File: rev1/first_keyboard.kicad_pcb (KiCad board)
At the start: 2 copper layers, 300 x 88.1 mm, 83 parts, among them SW1 SW_Push, SW10 SW_Push, SW11 SW_Push, SW12 SW_Push, SW13 SW_Push, SW14 SW_Push, SW15 SW_Push, SW16 SW_Push, SW17 SW_Push, SW18 SW_Push, SW19 SW_Push, SW2 SW_Push, SW20 SW_Push, SW21 SW_Push, SW22 SW_Push, SW23 SW_Push, SW24 SW_Push, SW25 SW_Push, SW26 SW_Push, SW27 SW_Push, SW28 SW_Push, SW29 SW_Push, SW3 SW_Push, SW30 SW_Push, SW31 SW_Push, SW32 SW_Push, SW33 SW_Push, SW34 SW_Push, SW35 SW_Push, SW36 SW_Push, SW37 SW_Push, SW38 SW_Push, SW39 SW_Push, SW4 SW_Push, SW40 SW_Push, SW41 SW_Push, SW5 SW_Push, SW6 SW_Push, SW7 SW_Push, SW8 SW_Push, SW9 SW_Push, U1 Pico

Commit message: feat: ダイオード位置変更
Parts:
- moved D41 7.31 mm to (357.2, 167.6)
- moved D22 2.85 mm to (266.7, 134.3)
- moved D23 2.85 mm to (266.7, 153.4)
- moved D24 2.85 mm to (266.7, 172.4)
- moved D27 2.85 mm to (285.8, 148.6)
- moved D30 2.85 mm to (285.8, 186.7)
- moved D40 2.85 mm to (361.9, 134.3)
- moved D26 2.85 mm to (285.8, 129.5)
- moved D1 2.85 mm to (85.7, 134.3)
- moved D2 2.85 mm to (85.7, 153.4)
- moved D3 2.85 mm to (85.7, 172.4)
- moved D28 2.85 mm to (285.8, 167.6)
- moved D29 2.85 mm to (266.7, 191.5)
- moved D11 2.85 mm to (142.9, 148.6)
- moved D13 2.85 mm to (161.9, 186.7)
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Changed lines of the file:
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@@
 	(footprint "kbd_Parts:Diode_TH_SMD"
 		(layer "F.Cu")
-		(at 326.23125 147.03125 90)
+		(at 323.85 148.59 90)
 		(descr "Resitance 3 pas")
 		(tags "R")
@@
 	(footprint "kbd_Parts:Diode_TH_SMD"
 		(layer "F.Cu")
-		(at 164.30625 185.13125 90)
+		(at 161.925 186.69 90)
 		(descr "Resitance 3 pas")
 		(tags "R")
@@
 	(footprint "kbd_Parts:Diode_TH_SMD"
 		(layer "F.Cu")
-		(at 269.08125 132.74375 90)
+		(at 266.7 134.3025 90)
 		(descr "Resitance 3 pas")
 		(tags "R")
@@
 	(footprint "kbd_Parts:Diode_TH_SMD"
 		(layer "F.Cu")
-		(at 107.15625 166.08125 90)
+		(at 104.775 167.64 90)
 		(descr "Resitance 3 pas")
 		(tags "R")
@@
 	(footprint "kbd_Parts:Diode_TH_SMD"
 		(layer "F.Cu")
-		(at 183.35625 132.74375 90)
+		(at 180.975 134.3025 90)
 		(descr "Resitance 3 pas")
 		(tags "R")
@@
 	(footprint "kbd_Parts:Diode_TH_SMD"
 		(layer "F.Cu")
-		(at 145.25625 166.08125 90)
+		(at 142.875 167.64 90)
 		(descr "Resitance 3 pas")
 		(tags "R")
@@
 	(footprint "kbd_Parts:Diode_TH_SMD"
 		(layer "F.Cu")
-		(at 107.15625 127.98125 90)
+		(at 104.775 129.54 90)
 		(descr "Resitance 3 pas")
 		(tags "R")
@@
 	(footprint "kbd_Parts:Diode_TH_SMD"
 		(layer "F.Cu")
-		(at 126.20625 147.03125 90)
+		(at 123.825 148.59 90)
 		(descr "Resitance 3 pas")
 		(tags "R")
@@
 	(footprint "kbd_Parts:Diode_TH_SMD"
 		(layer "F.Cu")
-		(at 202.40625 192.275 90)
+		(at 200.025 193.83375 90)
 		(descr "Resitance 3 pas")
 		(tags "R")
@@
 	(footprint "kbd_Parts:Diode_TH_SMD"
 		(layer "F.Cu")
-		(at 88.10625 151.79375 90)
+		(at 85.725 153.3525 90)
 		(descr "Resitance 3 pas")
 		(tags "R")
@@
 	(footprint "kbd_Parts:Diode_TH_SMD"
 		(layer "F.Cu")
-		(at 126.20625 127.98125 90)
+		(at 123.825 129.54 90)
 		(descr "Resitance 3 pas")
 		(tags "R")
@@
 	(footprint "kbd_Parts:Diode_TH_SMD"
 		(layer "F.Cu")
-		(at 126.20625 166.08125 90)
+		(at 123.825 167.64 90)
 		(descr "Resitance 3 pas")
 		(tags "R")
@@
 	(footprint "kbd_Parts:Diode_TH_SMD"
 		(layer "F.Cu")
-		(at 250.03125 192.275 90)
+		(at 247.65 193.83375 90)
 		(descr "Resitance 3 pas")
 		(tags "R")
@@
 	(footprint "kbd_Parts:Diode_TH_SMD"
 		(layer "F.Cu")
-		(at 288.13125 166.08125 90)
+		(at 285.75 167.64 90)
 		(descr "Resitance 3 pas")
 		(tags "R")
@@
 	(footprint "kbd_Parts:Diode_TH_SMD"
 		(layer "F.Cu")
-		(at 88.10625 170.84375 90)
+		(at 85.725 172.4025 90)
 		(descr "Resitance 3 pas")
 		(tags "R")
@@
 	(footprint "kbd_Parts:Diode_TH_SMD"
 		(layer "F.Cu")
-		(at 183.35625 170.84375 90)
+		(at 180.975 172.4025 90)
 		(descr "Resitance 3 pas")
 		(tags "R")
@@
 	(footprint "kbd_Parts:Diode_TH_SMD"
 		(layer "F.Cu")
-		(at 164.30625 147.03125 90)
+		(at 161.925 148.59 90)
 		(descr "Resitance 3 pas")
 		(tags "R")
@@
 	(footprint "kbd_Parts:Diode_TH_SMD"
 		(layer "F.Cu")
-		(at 326.23125 166.08125 90)
+		(at 323.85 167.64 90)
 		(descr "Resitance 3 pas")
 		(tags "R")
@@
 	(footprint "kbd_Parts:Diode_TH_SMD"
 		(layer "F.Cu")
-		(at 342.9 147.03125 90)
+		(at 342.9 148.59 90)
 		(descr "Resitance 3 pas")
 		(tags "R")
@@
 	(footprint "kbd_Parts:Diode_TH_SMD"
 		(layer "F.Cu")
-		(at 145.25625 147.03125 90)
+		(at 142.875 148.59 90)
 		(descr "Resitance 3 pas")
 		(tags "R")
@@
 	(footprint "kbd_Parts:Diode_TH_SMD"
 		(layer "F.Cu")
-		(at 288.13125 147.03125 90)
+		(at 285.75 148.59 90)
 		(descr "Resitance 3 pas")
 		(tags "R")
@@
 	(footprint "kbd_Parts:Diode_TH_SMD"
 		(layer "F.Cu")
-		(at 288.13125 127.98125 90)
+		(at 285.75 129.54 90)
 		(descr "Resitance 3 pas")
 		(tags "R")
@@
 	(footprint "kbd_Parts:Diode_TH_SMD"
 		(layer "F.Cu")
-		(at 183.35625 189.89375 90)
+		(at 180.975 191.4525 90)
 		(descr "Resitance 3 pas")
 		(tags "R")
@@
 	(footprint "kbd_Parts:Diode_TH_SMD"
 		(layer "F.Cu")
-		(at 307.18125 147.03125 90)
+		(at 304.8 148.59 90)
 		(descr "Resitance 3 pas")
 		(tags "R")
@@
 	(footprint "kbd_Parts:Diode_TH_SMD"
 		(layer "F.Cu")
-		(at 342.9 127.98125 90)
+		(at 342.9 129.54 90)
 		(descr "Resitance 3 pas")
 		(tags "R")
@@
 	(footprint "kbd_Parts:Diode_TH_SMD"
 		(layer "F.Cu")
-		(at 145.25625 127.98125 90)
+		(at 142.875 129.54 90)
 		(descr "Resitance 3 pas")
 		(tags "R")
@@
 	(footprint "kbd_Parts:Diode_TH_SMD"
 		(layer "F.Cu")
-		(at 364.33125 132.74375 90)
+		(at 361.95 134.3025 90)
 		(descr "Resitance 3 pas")
 		(tags "R")
@@
 	(footprint "kbd_Parts:Diode_TH_SMD"
 		(layer "F.Cu")
-		(at 342.9 166.08125 90)
+		(at 342.9 167.64 90)
 		(descr "Resitance 3 pas")
 		(tags "R")
@@
 	(footprint "kbd_Parts:Diode_TH_SMD"
 		(layer "F.Cu")
-		(at 183.35625 151.79375 90)
+		(at 180.975 153.3525 90)
 		(descr "Resitance 3 pas")
 		(tags "R")
@@
 	(footprint "kbd_Parts:Diode_TH_SMD"
 		(layer "F.Cu")
-		(at 107.15625 147.03125 90)
+		(at 104.775 148.59 90)
 		(descr "Resitance 3 pas")
 		(tags "R")
@@
 	(footprint "kbd_Parts:Diode_TH_SMD"
 		(layer "F.Cu")
-		(at 307.18125 127.98125 90)
+		(at 304.8 129.54 90)
 		(descr "Resitance 3 pas")
 		(tags "R")
@@
 	(footprint "kbd_Parts:Diode_TH_SMD"
 		(layer "F.Cu")
-		(at 326.23125 127.98125 90)
+		(at 323.85 129.54 90)
 		(descr "Resitance 3 pas")
 		(tags "R")
@@
 	(footprint "kbd_Parts:Diode_TH_SMD"
 		(layer "F.Cu")
-		(at 88.10625 132.74375 90)
+		(at 85.725 134.3025 90)
 		(descr "Resitance 3 pas")
 		(tags "R")
@@
 	(footprint "kbd_Parts:Diode_TH_SMD"
 		(layer "F.Cu")
-		(at 307.18125 166.08125 90)
+		(at 304.8 167.64 90)
 		(descr "Resitance 3 pas")
 		(tags "R")
@@
 	(footprint "kbd_Parts:Diode_TH_SMD"
 		(layer "F.Cu")
-		(at 269.08125 170.84375 90)
+		(at 266.7 172.4025 90)
 		(descr "Resitance 3 pas")
 		(tags "R")
@@
 	(footprint "kbd_Parts:Diode_TH_SMD"
 		(layer "F.Cu")
-		(at 269.08125 189.89375 90)
+		(at 266.7 191.4525 90)
 		(descr "Resitance 3 pas")
 		(tags "R")
@@
 	(footprint "kbd_Parts:Diode_TH_SMD"
 		(layer "F.Cu")
-		(at 269.08125 151.79375 90)
+		(at 266.7 153.3525 90)
 		(descr "Resitance 3 pas")
 		(tags "R")
@@
 	(footprint "kbd_Parts:Diode_TH_SMD"
 		(layer "F.Cu")
-		(at 164.30625 127.98125 90)
+		(at 161.925 129.54 90)
 		(descr "Resitance 3 pas")
 		(tags "R")
@@
 	(footprint "kbd_Parts:Diode_TH_SMD"
 		(layer "F.Cu")
-		(at 364.33125 166.08125 90)
+		(at 357.1875 167.64 90)
 		(descr "Resitance 3 pas")
 		(tags "R")
@@
 	(footprint "kbd_Parts:Diode_TH_SMD"
 		(layer "F.Cu")
-		(at 164.30625 166.08125 90)
+		(at 161.925 167.64 90)
 		(descr "Resitance 3 pas")
 		(tags "R")
@@
 	(footprint "kbd_Parts:Diode_TH_SMD"
 		(layer "F.Cu")
-		(at 288.13125 185.13125 90)
+		(at 285.75 186.69 90)
 		(descr "Resitance 3 pas")
 		(tags "R")
@@
 		(layer "Edge.Cuts")
 	)
-	(dimension
-		(type aligned)
-		(layer "F.Cu")
-		(pts
-			(xy 250.03125 138.1125) (xy 216.69375 138.1125)
-		)
-		(height 0)
-		(gr_text "33.3375 mm"
-			(at 233.3625 136.3125 0)
-			(layer "F.Cu")
-			(effects
-				(font
-					(size 1.5 1.5)
-					(thickness 0.3)
-				)
-			)
-		)
-		(format
-			(prefix "")
-			(suffix "")
-			(units 3)
-			(units_format 1)
-			(precision 4)
-		)
-		(style
-			(thickness 0.2)
-			(arrow_length 1.27)
-			(text_position_mode 0)
-			(extension_height 0.58642)
-			(extension_offset 0.5) keep_text_aligned)
-	)
-	(dimension
-		(type aligned)
-		(layer "F.Cu")
-		(pts
-			(xy 183.35625 138.1125) (xy 216.69375 138.1125)
-		)
-		(height 0)
-		(gr_text "33.3375 mm"
-			(at 200.025 136.3125 0)
-			(layer "F.Cu")
-			(effects
-				(font
-					(size 1.5 1.5)
-					(thickness 0.3)
-				)
-			)
-		)
-		(format
-			(prefix "")
-			(suffix "")
-			(units 3)
-			(units_format 1)
-			(precision 4)
-		)
-		(style
-			(thickness 0.2)
-			(arrow_length 1.27)
-			(text_position_mode 0)
-			(extension_height 0.58642)
-			(extension_offset 0.5) keep_text_aligned)
-	)
 )

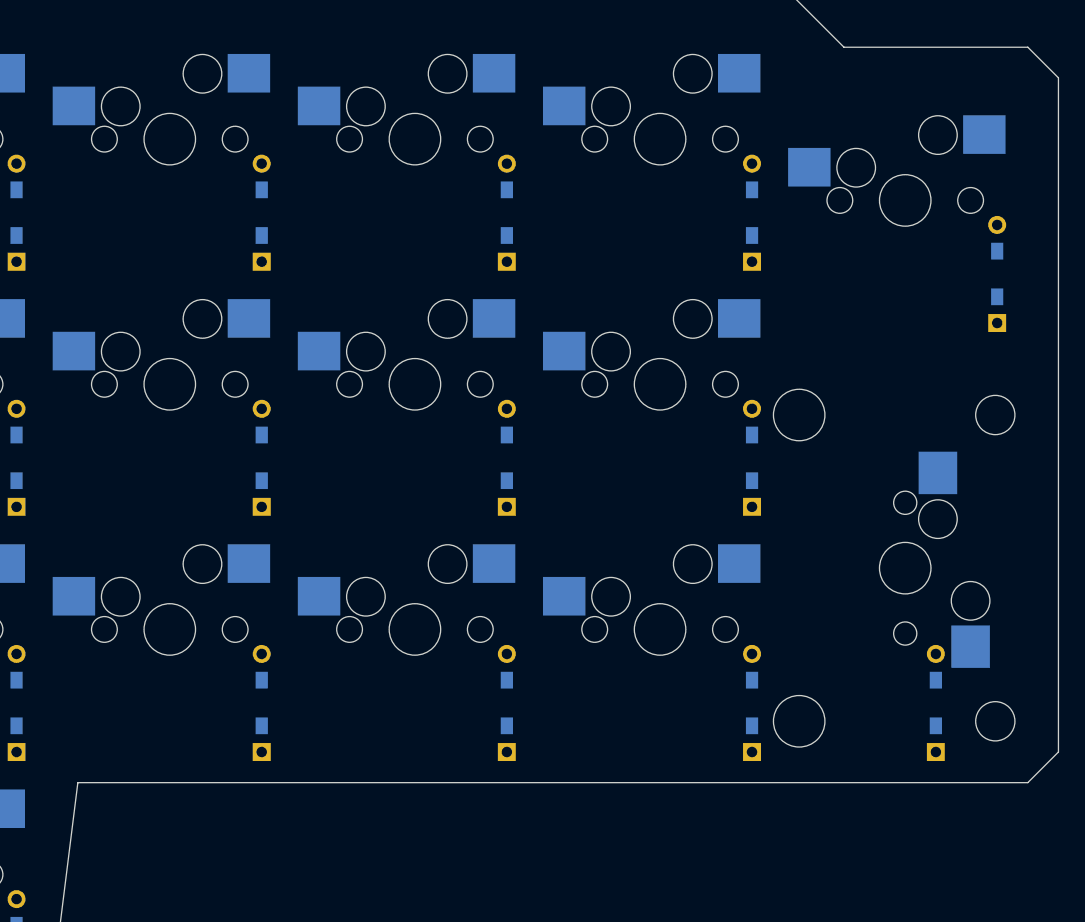
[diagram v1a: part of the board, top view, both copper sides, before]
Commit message: feat: 輪郭線変更
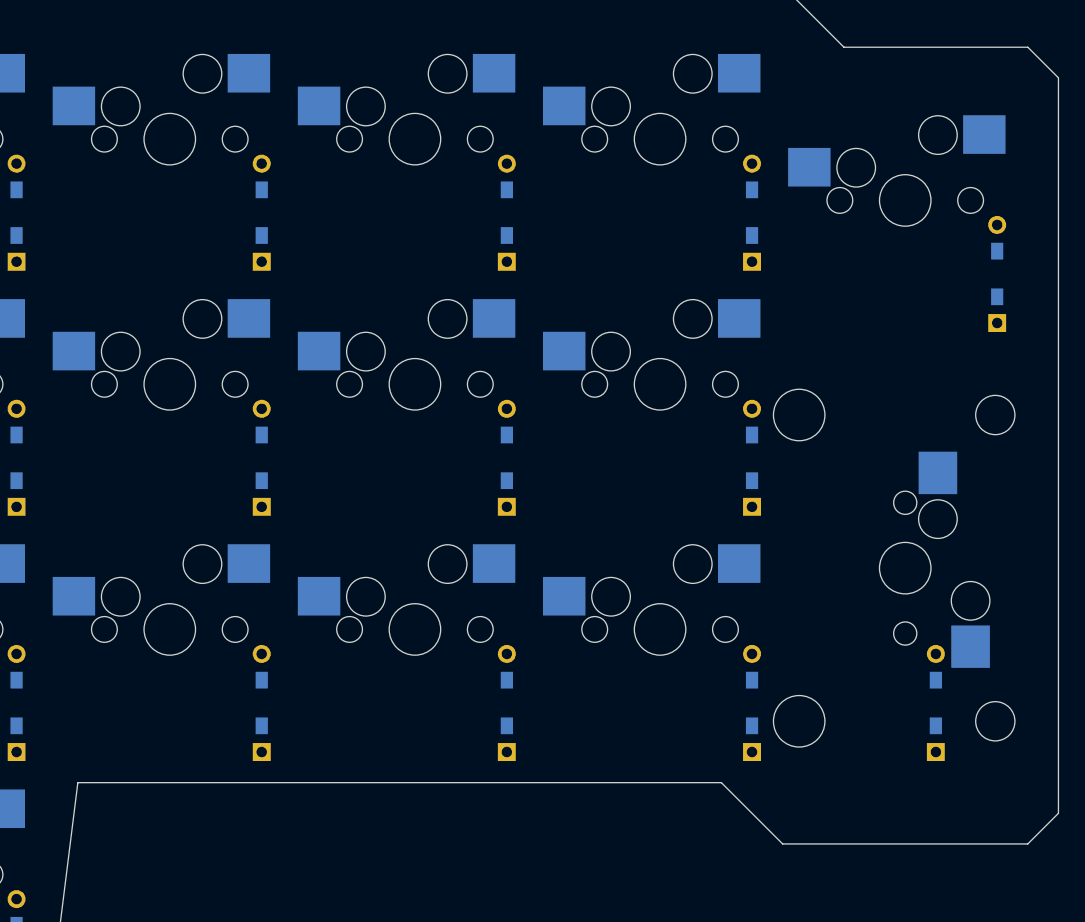
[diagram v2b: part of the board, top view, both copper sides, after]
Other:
- outline, holes or cut-outs redrawn
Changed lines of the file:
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@@
 	)
 	(gr_line
-		(start 366.7125 171.45)
+		(start 366.7125 176.2125)
 		(end 366.7125 119.0625)
 		(stroke
@@
 	)
 	(gr_line
+		(start 345.28125 178.59375)
+		(end 364.33125 178.59375)
+		(stroke
+			(width 0.1)
+			(type default)
+		)
+		(layer "Edge.Cuts")
+	)
+	(gr_line
 		(start 216.69375 111.91875)
 		(end 233.3625 111.91875)
@@
 	)
 	(gr_line
-		(start 364.33125 173.83125)
-		(end 366.7125 171.45)
-		(stroke
-			(width 0.1)
-			(type default)
-		)
-		(layer "Edge.Cuts")
-	)
-	(gr_line
 		(start 66.675 119.0625)
 		(end 66.675 176.2125)
@@
 	)
 	(gr_line
+		(start 366.7125 176.2125)
+		(end 364.33125 178.59375)
+		(stroke
+			(width 0.1)
+			(type default)
+		)
+		(layer "Edge.Cuts")
+	)
+	(gr_line
 		(start 164.30625 111.91875)
 		(end 88.10625 111.91875)
@@
 	(gr_line
 		(start 290.5125 173.83125)
-		(end 364.33125 173.83125)
-		(stroke
-			(width 0.1)
+		(end 340.51875 173.83125)
+		(stroke
+			(width 0.1)
+			(type default)
+		)
+		(layer "Edge.Cuts")
+	)
+	(gr_line
+		(start 340.51875 173.83125)
+		(end 345.28125 178.59375)
+		(stroke
+			(width 0.1)

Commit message: feat: スペース繋げて外形変更
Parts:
- moved D34 28.6 mm to (295.3, 129.5)
- moved D35 28.6 mm to (295.3, 148.6)
- moved D36 28.6 mm to (295.3, 167.6)
- moved SW37 28.6 mm to (307.2, 123.8)
- moved SW38 28.6 mm to (307.2, 142.9)
- moved SW39 28.6 mm to (307.2, 161.9)
- moved D25 28.6 mm to (219.1, 193.8)
- moved D22 28.6 mm to (238.1, 134.3)
- moved D23 28.6 mm to (238.1, 153.4)
- moved D24 28.6 mm to (238.1, 172.4)
- moved D26 28.6 mm to (257.2, 129.5)
- moved D27 28.6 mm to (257.2, 148.6)
- moved D28 28.6 mm to (257.2, 167.6)
- moved D29 28.6 mm to (238.1, 191.5)
- moved D30 28.6 mm to (257.2, 186.7)
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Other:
- board size 300 x 88.1 mm -> 271.5 x 88.1 mm

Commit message: feat: ダイオード実装面変更
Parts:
- D1, D10, D11, D12, D13, D14, D15, D16, D17, D18, D19, D2, D20, D21, D22, D23, D24, D25, D26, D27, D28, D29, D3, D30, D31, D32, D33, D34, D35, D36, D37, D38, D39, D4, D40, D41, D5, D6, D7, D8, D9: moved to B.Cu
- moved D10 1.43 mm to (141.4, 129.5)
- moved D11 1.43 mm to (141.4, 148.6)
- moved D12 1.43 mm to (141.4, 167.6)
- moved D13 1.43 mm to (160.5, 186.7)
- moved D14 1.43 mm to (160.5, 129.5)
- moved D15 1.43 mm to (160.5, 148.6)
- moved D16 1.43 mm to (160.5, 167.6)
- moved D17 1.43 mm to (179.5, 191.5)
- moved D18 1.43 mm to (179.5, 134.3)
- moved D19 1.43 mm to (179.5, 153.4)
- moved D20 1.43 mm to (179.5, 172.4)
- moved D22 1.43 mm to (236.7, 134.3)
- moved D23 1.43 mm to (236.7, 153.4)
- moved D24 1.43 mm to (236.7, 172.4)
- moved D26 1.43 mm to (255.7, 129.5)
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
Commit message: feat: ６角スペーサー穴追加
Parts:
- added Ref**: Val**, kbd_Hole:m2_Spacer_Hole_hex, F.Cu at (162.5, 192.0)
- added Ref**: Val**, kbd_Hole:m2_Spacer_Hole_hex, F.Cu at (242.5, 192.0)
- added Ref**: Val**, kbd_Hole:m2_Spacer_Hole_hex, F.Cu at (318.5, 117.0)
- added Ref**: Val**, kbd_Hole:m2_Spacer_Hole_hex, F.Cu at (86.5, 117.0)
- added Ref**: Val**, kbd_Hole:m2_Spacer_Hole_hex, F.Cu at (314.5, 173.0)
- added Ref**: Val**, kbd_Hole:m2_Spacer_Hole_hex, F.Cu at (90.5, 173.0)
- added Ref**: Val**, kbd_Hole:m2_Spacer_Hole_hex, F.Cu at (238.5, 117.0)
- added Ref**: Val**, kbd_Hole:m2_Spacer_Hole_hex, F.Cu at (166.5, 117.0)
- moved D13 4.19 mm to (161.9, 182.8)

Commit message: feat: pcbのネジ穴にRevを振る
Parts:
- renumbered Ref** to Ref1, Ref** to Ref2, Ref** to Ref3, Ref** to Ref4, Ref** to Ref5, Ref** to Ref6, Ref** to Ref7, Ref** to Ref8
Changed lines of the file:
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@@
 		(descr "Mounting Hole 2.2mm, no annular, M2")
 		(tags "mounting hole 2.2mm no annular m2")
-		(property "Reference" "Ref**"
+		(property "Reference" "Ref3"
 			(at 0 -3.2 0)
 			(layer "F.Fab")
@@
 		(descr "Mounting Hole 2.2mm, no annular, M2")
 		(tags "mounting hole 2.2mm no annular m2")
-		(property "Reference" "Ref**"
+		(property "Reference" "Ref6"
 			(at 0 -3.2 0)
 			(layer "F.Fab")
@@
 		(descr "Mounting Hole 2.2mm, no annular, M2")
 		(tags "mounting hole 2.2mm no annular m2")
-		(property "Reference" "Ref**"
+		(property "Reference" "Ref8"
 			(at 0 -3.2 0)
 			(layer "F.Fab")
@@
 		(descr "Mounting Hole 2.2mm, no annular, M2")
 		(tags "mounting hole 2.2mm no annular m2")
-		(property "Reference" "Ref**"
+		(property "Reference" "Ref1"
 			(at 0 -3.2 0)
 			(layer "F.Fab")
@@
 		(descr "Mounting Hole 2.2mm, no annular, M2")
 		(tags "mounting hole 2.2mm no annular m2")
-		(property "Reference" "Ref**"
+		(property "Reference" "Ref7"
 			(at 0 -3.2 0)
 			(layer "F.Fab")
@@
 		(descr "Mounting Hole 2.2mm, no annular, M2")
 		(tags "mounting hole 2.2mm no annular m2")
-		(property "Reference" "Ref**"
+		(property "Reference" "Ref2"
 			(at 0 -3.2 0)
 			(layer "F.Fab")
@@
 		(descr "Mounting Hole 2.2mm, no annular, M2")
 		(tags "mounting hole 2.2mm no annular m2")
-		(property "Reference" "Ref**"
+		(property "Reference" "Ref5"
 			(at 0 -3.2 0)
 			(layer "F.Fab")
@@
 		(descr "Mounting Hole 2.2mm, no annular, M2")
 		(tags "mounting hole 2.2mm no annular m2")
-		(property "Reference" "Ref**"
+		(property "Reference" "Ref4"
 			(at 0 -3.2 0)
 			(layer "F.Fab")

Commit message: feat: 配線
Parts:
- moved D39 4.19 mm to (314.3, 163.7)
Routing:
- net Row0: track 0.00 -> 412.3 mm, vias 0 -> 1
- net Row1: track 0.00 -> 311.8 mm, vias 0 -> 1
- net Row2: track 0.00 -> 284.3 mm, vias 0 -> 1
- net Row3: track 0.00 -> 174.4 mm
- net Col0: track 0.00 -> 168.2 mm, vias 0 -> 1
- net Col11: track 0.00 -> 151.7 mm, vias 0 -> 1
- net Col10: track 0.00 -> 151.4 mm
- net Col1: track 0.00 -> 144.8 mm, vias 0 -> 1
- net Col2: track 0.00 -> 125.5 mm, vias 0 -> 1
- net Col3: track 0.00 -> 124.1 mm, vias 0 -> 1
- net Col4: track 0.00 -> 115.8 mm, vias 0 -> 1
- net Col9: track 0.00 -> 109.3 mm, vias 0 -> 1
- net Col8: track 0.00 -> 108.2 mm
- net Col7: track 0.00 -> 99.9 mm, vias 0 -> 1
- net Col5: track 0.00 -> 95.0 mm
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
